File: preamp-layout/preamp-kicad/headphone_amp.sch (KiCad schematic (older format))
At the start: 4 parts, among them J10 Conn_01x02_Female, J11 Conn_01x03_Male, J12 Conn_01x03_Female, J9 Conn_01x02_Male

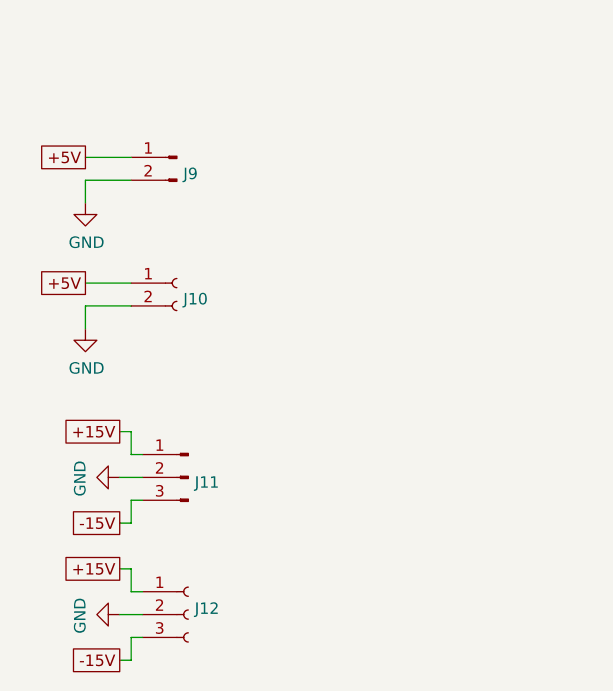
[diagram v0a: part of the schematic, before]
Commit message: AC PCB Update
Removed Switch symbol from PCB, moved to main sheet. Started playing with footprint assignment. Other minor updates.
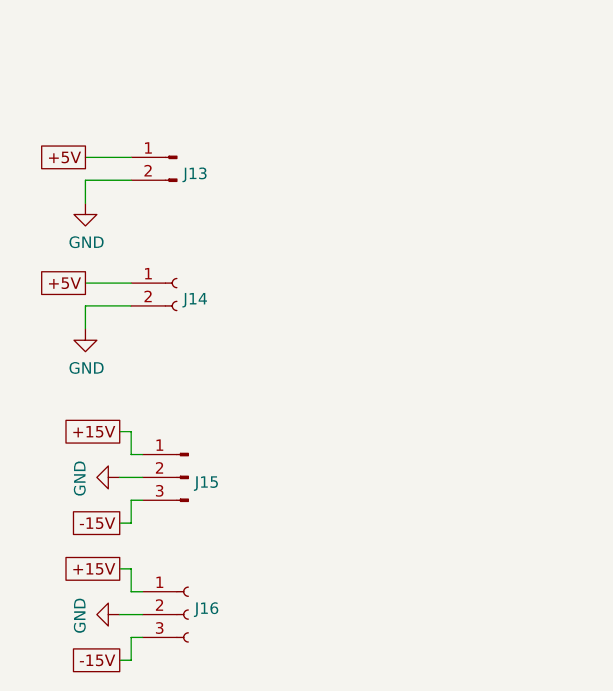
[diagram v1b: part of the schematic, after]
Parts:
- renumbered J9 to J13, J10 to J14, J11 to J15, J12 to J16
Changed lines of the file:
@@
 AR Path="/5E5EF2D4/60B7C07D" Ref="J?"  Part="1"
 AR Path="/6009D432/60B7C07D" Ref="J?"  Part="1"
-AR Path="/5E4A803E/60B7C07D" Ref="J9"  Part="1"
-F 0 "J9" H 1672 5228 50  0000 R CNN
+AR Path="/5E4A803E/60B7C07D" Ref="J13"  Part="1"
+F 0 "J13" H 1672 5228 50  0000 R CNN
 F 1 "Conn_01x02_Male" H 1672 5183 50  0001 R CNN
 F 2 "" H 1700 5300 50  0001 C CNN
@@
 P 1700 5850
 AR Path="/6009D432/60B7C0A9" Ref="J?"  Part="1"
-AR Path="/5E4A803E/60B7C0A9" Ref="J10"  Part="1"
-F 0 "J10" H 1728 5780 50  0000 L CNN
+AR Path="/5E4A803E/60B7C0A9" Ref="J14"  Part="1"
+F 0 "J14" H 1728 5780 50  0000 L CNN
 F 1 "Conn_01x02_Female" H 1728 5735 50  0001 L CNN
 F 2 "" H 1700 5850 50  0001 C CNN
@@
 AR Path="/5E27B612/647A3EBE" Ref="J?"  Part="1"
 AR Path="/6009D432/647A3EBE" Ref="J?"  Part="1"
-AR Path="/5E4A803E/647A3EBE" Ref="J11"  Part="1"
-F 0 "J11" H 1722 6678 50  0000 R CNN
+AR Path="/5E4A803E/647A3EBE" Ref="J15"  Part="1"
+F 0 "J15" H 1722 6678 50  0000 R CNN
 F 1 "Conn_01x03_Male" H 1722 6633 50  0001 R CNN
 F 2 "" H 1750 6700 50  0001 C CNN
@@
 AR Path="/5E2D8DA2/647A3EC4" Ref="J?"  Part="1"
 AR Path="/6009D432/647A3EC4" Ref="J?"  Part="1"
-AR Path="/5E4A803E/647A3EC4" Ref="J12"  Part="1"
-F 0 "J12" H 1778 7326 50  0000 L CNN
+AR Path="/5E4A803E/647A3EC4" Ref="J16"  Part="1"
+F 0 "J16" H 1778 7326 50  0000 L CNN
 F 1 "Conn_01x03_Female" H 1778 7235 50  0001 L CNN
 F 2 "" H 1750 7300 50  0001 C CNN

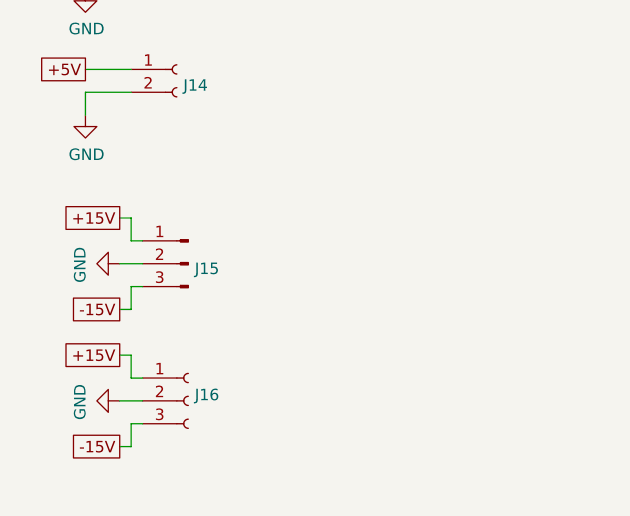
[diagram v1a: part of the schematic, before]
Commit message: BOM update
Minor changes to schematic, value changes and footprint entry. BOM updated with parts sourcing
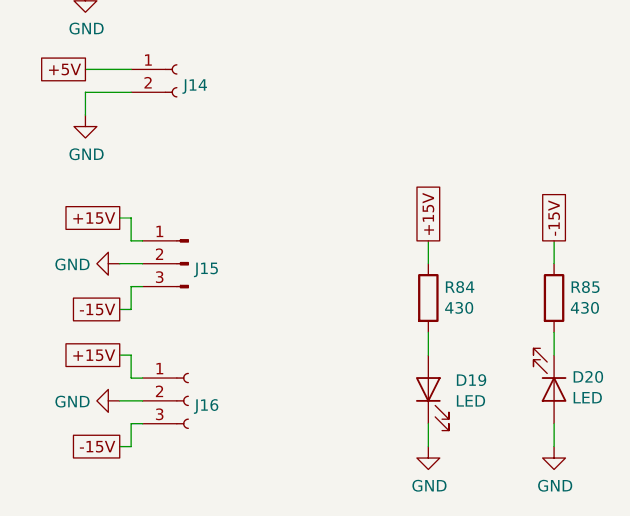
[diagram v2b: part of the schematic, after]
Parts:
- added D19, D20: LED, LED_SMD:LED_1206_3216Metric_Pad1.42x1.75mm_HandSolder, symbol Device:LED
- added R84, R85: 430, Resistor_SMD:R_1206_3216Metric_Pad1.42x1.75mm_HandSolder, symbol Device:R
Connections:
- net +15V: now also R84.1
- net -15V: now also R85.1
- net GND: now also D19.1 (K), D20.2 (A)
- new net: D19.2 (A), R84.2
- new net: D20.1 (K), R85.2
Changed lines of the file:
@@
 AR Path="/6009D432/647A3EC4" Ref="J?"  Part="1"
 AR Path="/5E4A803E/647A3EC4" Ref="J16"  Part="1"
-F 0 "J16" H 1778 7326 50  0000 L CNN
+F 0 "J16" H 1778 7280 50  0000 L CNN
 F 1 "Conn_01x03_Female" H 1778 7235 50  0001 L CNN
 F 2 "" H 1750 7300 50  0001 C CNN
@@
 AR Path="/5E4A803E/64EC1E68" Ref="#PWR017"  Part="1"
 F 0 "#PWR017" H 1450 6450 50  0001 C CNN
-F 1 "GND" H 1455 6527 50  0000 C CNN
+F 1 "GND" V 1455 6572 50  0000 R CNN
 F 2 "" H 1450 6700 50  0001 C CNN
 F 3 "" H 1450 6700 50  0001 C CNN
@@
 AR Path="/5E4A803E/64EC22F8" Ref="#PWR018"  Part="1"
 F 0 "#PWR018" H 1450 7050 50  0001 C CNN
-F 1 "GND" H 1455 7127 50  0000 C CNN
+F 1 "GND" V 1455 7172 50  0000 R CNN
 F 2 "" H 1450 7300 50  0001 C CNN
 F 3 "" H 1450 7300 50  0001 C CNN
@@
 	0    1    1    0
 $EndComp
+Text GLabel 2800 6600 1    50   UnSpc ~ 0
++15V
+$Comp
+L Device:R R?
+U 1 1 5E3C1B26
+P 2800 6850
+AR Path="/5E2D8DA2/5E3C1B26" Ref="R?"  Part="1"
+AR Path="/5E3C1B26" Ref="R?"  Part="1"
+AR Path="/5E27B612/5E3C1B26" Ref="R?"  Part="1"
+AR Path="/6009D432/5E3C1B26" Ref="R?"  Part="1"
+AR Path="/5E4A803E/5E3C1B26" Ref="R84"  Part="1"
+F 0 "R84" H 2870 6896 50  0000 L CNN
+F 1 "430" H 2870 6805 50  0000 L CNN
+F 2 "Resistor_SMD:R_1206_3216Metric_Pad1.42x1.75mm_HandSolder" V 2730 6850 50  0001 C CNN
+F 3 "~" H 2800 6850 50  0001 C CNN
+	1    2800 6850
+	1    0    0    -1
+$EndComp
+$Comp
+L Device:LED D?
+U 1 1 5E3C1B2C
+P 2800 7250
+AR Path="/5E2D8DA2/5E3C1B2C" Ref="D?"  Part="1"
+AR Path="/5E27B612/5E3C1B2C" Ref="D?"  Part="1"
+AR Path="/6009D432/5E3C1B2C" Ref="D?"  Part="1"
+AR Path="/5E4A803E/5E3C1B2C" Ref="D19"  Part="1"
+F 0 "D19" V 2839 7132 50  0000 R CNN
+F 1 "LED" V 2748 7132 50  0000 R CNN
+F 2 "LED_SMD:LED_1206_3216Metric_Pad1.42x1.75mm_HandSolder" H 2800 7250 50  0001 C CNN
+F 3 "~" H 2800 7250 50  0001 C CNN
+	1    2800 7250
+	0    -1   -1   0
+$EndComp
+Wire Wire Line
+	2800 6600 2800 6700
+Wire Wire Line
+	2800 7000 2800 7100
+Wire Wire Line
+	2800 7400 2800 7500
+Text GLabel 3350 6600 1    50   UnSpc ~ 0
+-15V
+$Comp
+L Device:R R?
+U 1 1 5E3C1B36
+P 3350 6850
+AR Path="/5E2D8DA2/5E3C1B36" Ref="R?"  Part="1"
+AR Path="/5E3C1B36" Ref="R?"  Part="1"
+AR Path="/5E27B612/5E3C1B36" Ref="R?"  Part="1"
+AR Path="/6009D432/5E3C1B36" Ref="R?"  Part="1"
+AR Path="/5E4A803E/5E3C1B36" Ref="R85"  Part="1"
+F 0 "R85" H 3420 6896 50  0000 L CNN
+F 1 "430" H 3420 6805 50  0000 L CNN
+F 2 "Resistor_SMD:R_1206_3216Metric_Pad1.42x1.75mm_HandSolder" V 3280 6850 50  0001 C CNN
+F 3 "~" H 3350 6850 50  0001 C CNN
+	1    3350 6850
+	1    0    0    -1
+$EndComp
+$Comp
+L Device:LED D?
+U 1 1 5E3C1B3C
+P 3350 7250
+AR Path="/5E2D8DA2/5E3C1B3C" Ref="D?"  Part="1"
+AR Path="/5E27B612/5E3C1B3C" Ref="D?"  Part="1"
+AR Path="/6009D432/5E3C1B3C" Ref="D?"  Part="1"
+AR Path="/5E4A803E/5E3C1B3C" Ref="D20"  Part="1"
+F 0 "D20" V 3297 7329 50  0000 L CNN
+F 1 "LED" V 3388 7329 50  0000 L CNN
+F 2 "LED_SMD:LED_1206_3216Metric_Pad1.42x1.75mm_HandSolder" H 3350 7250 50  0001 C CNN
+F 3 "~" H 3350 7250 50  0001 C CNN
+	1    3350 7250
+	0    1    1    0
+$EndComp
+Wire Wire Line
+	3350 6600 3350 6700
+Wire Wire Line
+	3350 7000 3350 7100
+Wire Wire Line
+	3350 7400 3350 7500
+$Comp
+L power:GND #PWR?
+U 1 1 5E3C1B45
+P 2800 7500
+AR Path="/6009D432/5E3C1B45" Ref="#PWR?"  Part="1"
+AR Path="/5E4A803E/5E3C1B45" Ref="#PWR0107"  Part="1"
+F 0 "#PWR0107" H 2800 7250 50  0001 C CNN
+F 1 "GND" H 2805 7327 50  0000 C CNN
+F 2 "" H 2800 7500 50  0001 C CNN
+F 3 "" H 2800 7500 50  0001 C CNN
+	1    2800 7500
+	1    0    0    -1
+$EndComp
+$Comp
+L power:GND #PWR?
+U 1 1 5E3C1B4B
+P 3350 7500
+AR Path="/6009D432/5E3C1B4B" Ref="#PWR?"  Part="1"
+AR Path="/5E4A803E/5E3C1B4B" Ref="#PWR0108"  Part="1"
+F 0 "#PWR0108" H 3350 7250 50  0001 C CNN
+F 1 "GND" H 3355 7327 50  0000 C CNN
+F 2 "" H 3350 7500 50  0001 C CNN
+F 3 "" H 3350 7500 50  0001 C CNN
+	1    3350 7500
+	1    0    0    -1
+$EndComp
 $EndSCHEMATC

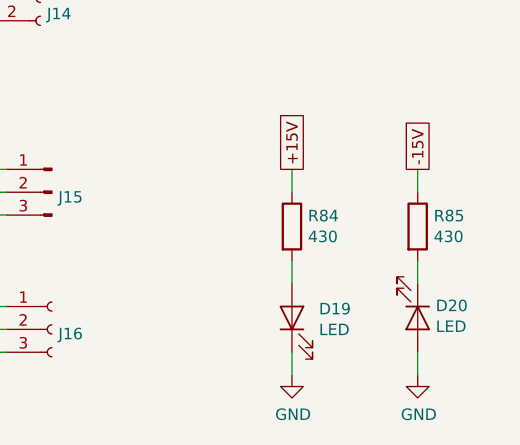
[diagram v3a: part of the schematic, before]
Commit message: LED resistor update
In the process of reviewing layouts and associated parts sourcing, I realized that I had incorrectly calculated the resistors needed for the power supply LEDs on all boards. Updated BOM and schematics to match. Other minor schematic updates.
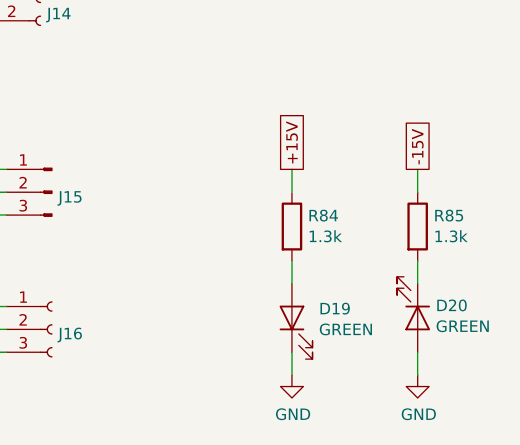
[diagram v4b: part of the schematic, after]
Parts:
- D19, D20: value LED -> GREEN
- R84, R85: value 430 -> 1.3k
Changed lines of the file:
@@
 AR Path="/5E4A803E/5E3C1B26" Ref="R84"  Part="1"
 F 0 "R84" H 2870 6896 50  0000 L CNN
-F 1 "430" H 2870 6805 50  0000 L CNN
+F 1 "1.3k" H 2870 6805 50  0000 L CNN
 F 2 "Resistor_SMD:R_1206_3216Metric_Pad1.42x1.75mm_HandSolder" V 2730 6850 50  0001 C CNN
 F 3 "~" H 2800 6850 50  0001 C CNN
@@
 AR Path="/5E4A803E/5E3C1B2C" Ref="D19"  Part="1"
 F 0 "D19" V 2839 7132 50  0000 R CNN
-F 1 "LED" V 2748 7132 50  0000 R CNN
+F 1 "GREEN" V 2748 7132 50  0000 R CNN
 F 2 "LED_SMD:LED_1206_3216Metric_Pad1.42x1.75mm_HandSolder" H 2800 7250 50  0001 C CNN
 F 3 "~" H 2800 7250 50  0001 C CNN
@@
 AR Path="/5E4A803E/5E3C1B36" Ref="R85"  Part="1"
 F 0 "R85" H 3420 6896 50  0000 L CNN
-F 1 "430" H 3420 6805 50  0000 L CNN
+F 1 "1.3k" H 3420 6805 50  0000 L CNN
 F 2 "Resistor_SMD:R_1206_3216Metric_Pad1.42x1.75mm_HandSolder" V 3280 6850 50  0001 C CNN
 F 3 "~" H 3350 6850 50  0001 C CNN
@@
 AR Path="/5E4A803E/5E3C1B3C" Ref="D20"  Part="1"
 F 0 "D20" V 3297 7329 50  0000 L CNN
-F 1 "LED" V 3388 7329 50  0000 L CNN
+F 1 "GREEN" V 3388 7329 50  0000 L CNN
 F 2 "LED_SMD:LED_1206_3216Metric_Pad1.42x1.75mm_HandSolder" H 3350 7250 50  0001 C CNN
 F 3 "~" H 3350 7250 50  0001 C CNN

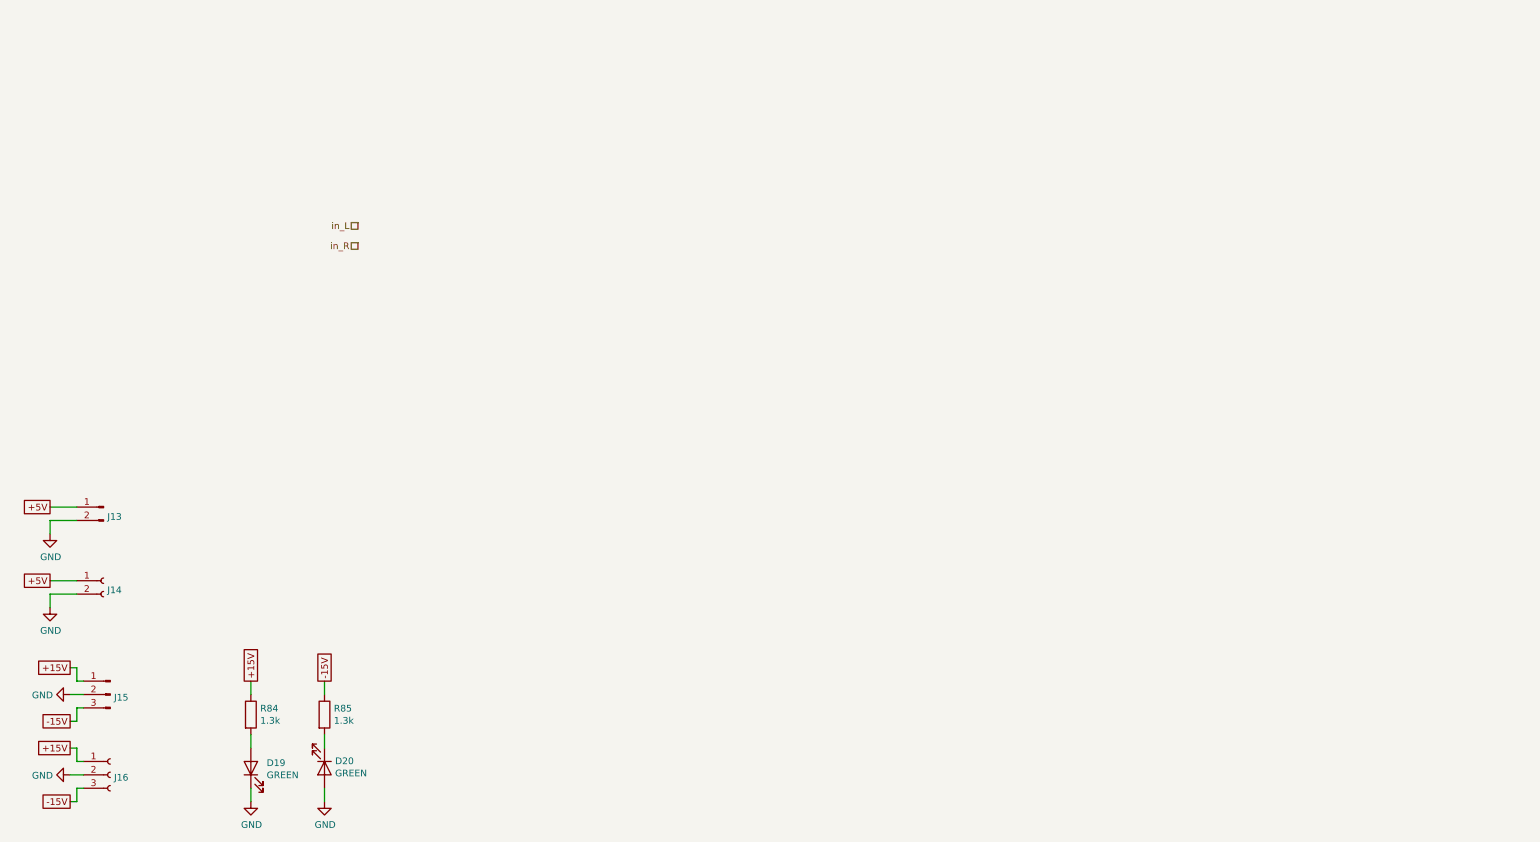
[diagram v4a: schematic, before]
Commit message: Update headphone_amp.sch
first draft of headphone amp
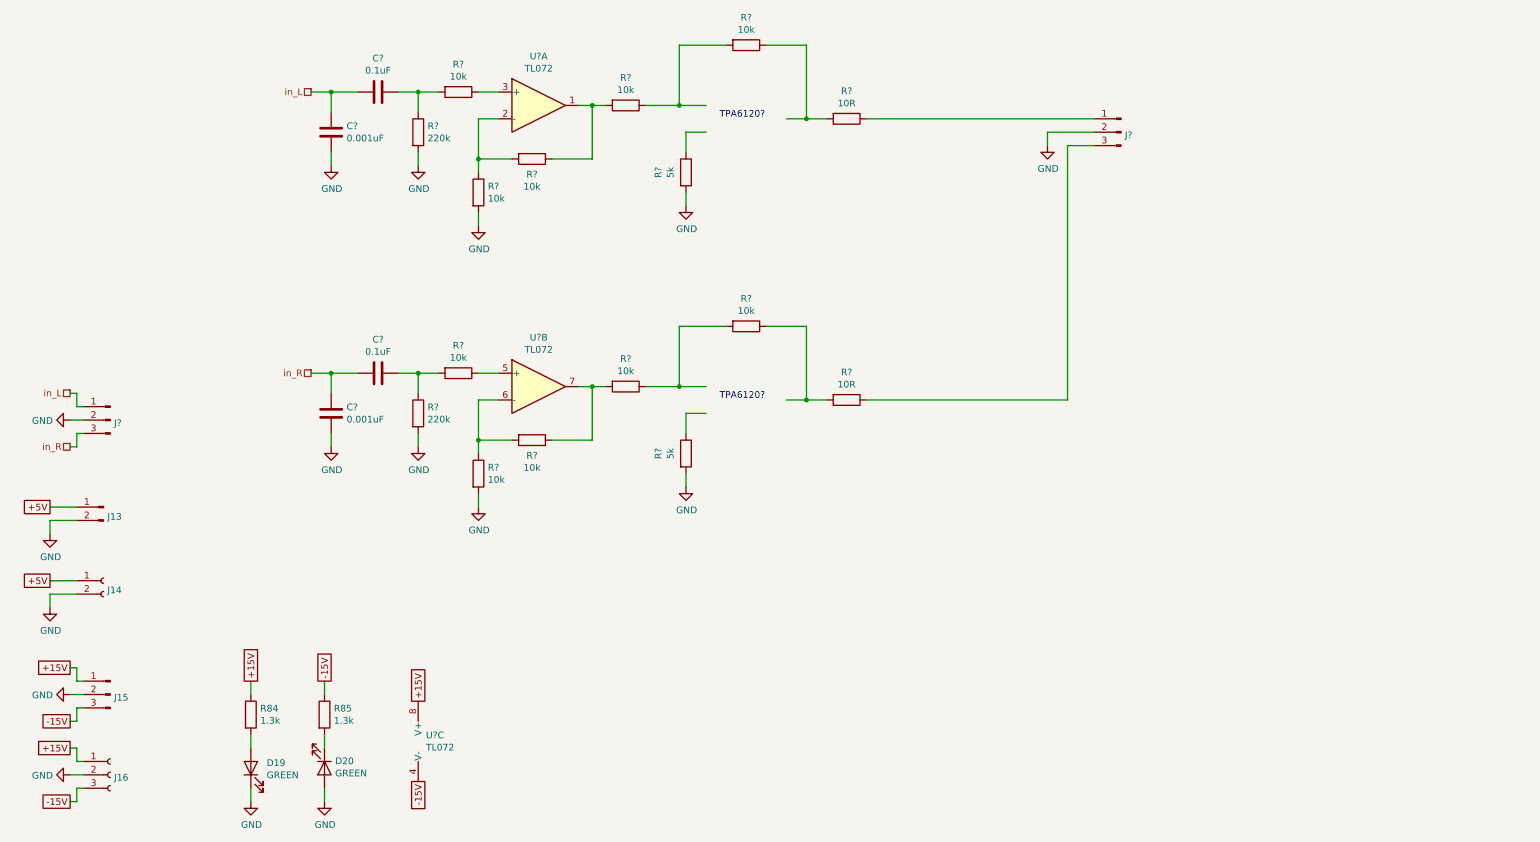
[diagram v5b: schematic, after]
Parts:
- added C? (x2): 0.001uF, symbol Device:C
- added C? (x2): 0.1uF, symbol Device:C
- added J? (x2): Conn_01x03_Male, symbol Connector:Conn_01x03_Male
- added R? (x10): 10k, Resistor_SMD:R_1206_3216Metric_Pad1.42x1.75mm_HandSolder, symbol Device:R
- added R? (x2): 220k, Resistor_SMD:R_1206_3216Metric_Pad1.42x1.75mm_HandSolder, symbol Device:R
- added R? (x2): 5k, Resistor_SMD:R_1206_3216Metric_Pad1.42x1.75mm_HandSolder, symbol Device:R
- added R? (x2): 10R, Resistor_SMD:R_1206_3216Metric_Pad1.42x1.75mm_HandSolder, symbol Device:R
- added U? (x2): TL072, Package_DIP:DIP-8_W7.62mm_Socket_LongPads, symbol Amplifier_Operational:TL072
- added U?: TL072, symbol Amplifier_Operational:TL072
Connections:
- wire segments 26 -> 97
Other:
- note added: "TPA6120?"

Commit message: Headphone Amp Crossfeed Implementation - using the CMOY modified Linkwitz High Z crossfeed design as a basis.
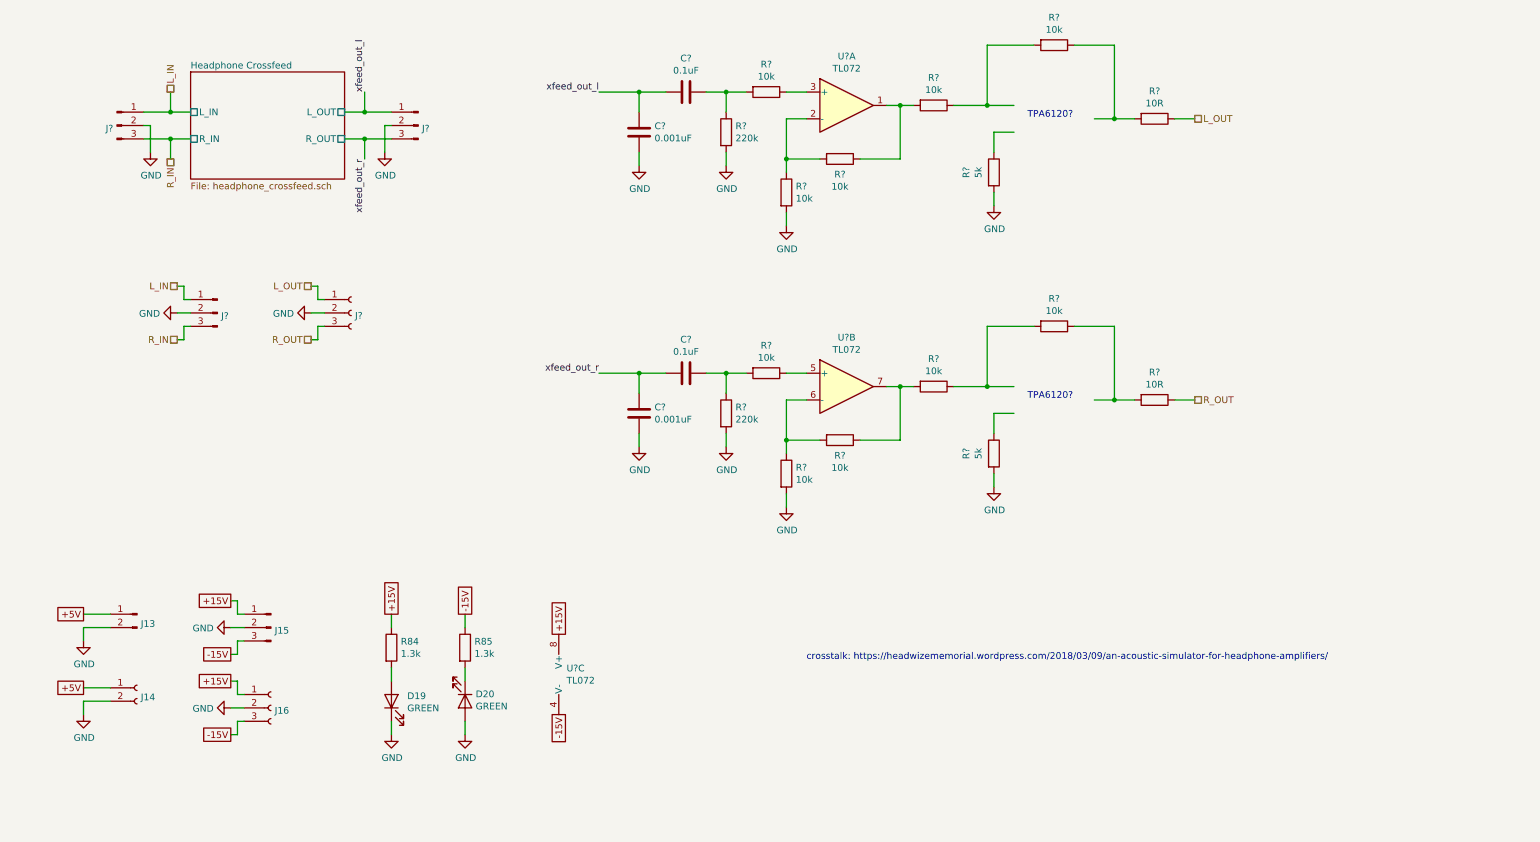
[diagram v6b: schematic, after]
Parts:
- removed J?: Conn_01x03_Male, symbol Connector:Conn_01x03_Male
- added J? (x2): Conn_01x03_Male, symbol Connector:Conn_01x03_Male
- added J?: Conn_01x03_Female, symbol Connector:Conn_01x03_Female
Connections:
- net labels added: L_IN, L_OUT, R_IN, R_OUT, xfeed_out_l, xfeed_out_r
- net labels removed: in_L, in_R
- wire segments 97 -> 116
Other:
- note added: "crosstalk: https://headwizememorial.wordpress.com/2018/03/09/an-acoustic-simulator-for-headphone-amplifiers/"
- moved on the sheet: C?, D19, D20, J13, J14, J15, J16, J?, R84, R85, R?, U?A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
